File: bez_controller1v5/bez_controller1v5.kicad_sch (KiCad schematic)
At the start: 75 parts, among them J1 Conn_01x03_Male, J10 IMU Conn_01x03_Female, J11 Conn_01x03_Male, J12 Conn_01x03_Male, J13 USB_B_Mini, J2 Conn_01x03_Male, J3 Conn_01x03_Male, J4 Screw_Terminal_01x02, J5 Conn_01x03_Male, J6 Conn_01x03_Male, J7 Conn_01x03_Male, J8 JTAG Conn_01x06_Male, J9 IMU Conn_01x08_Female, U1 PX07806-500-S, U10 USBLC6-4SC6, U11 74LVC2G241, U12 74LVC2G241, U2 74LVC2G241, U3 74LVC2G241, U4 LF50ABV_TO220, U5 LD1117AS33TR_SOT223, U6 INA180A1, U7 STM32F446RETx, U8 74LVC2G241, U9 74LVC2G241, Y1 8MHz

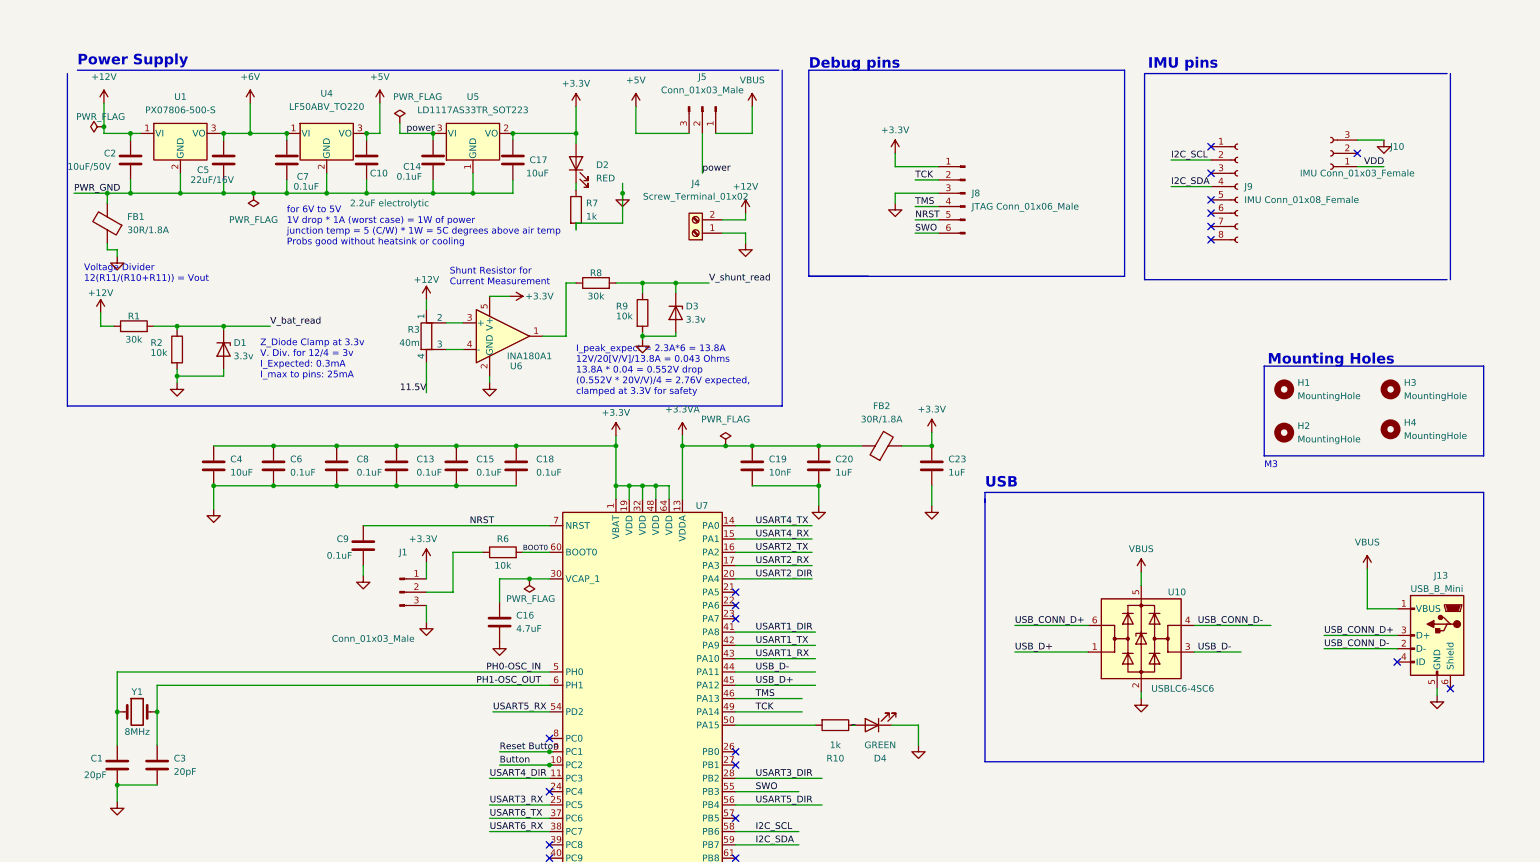
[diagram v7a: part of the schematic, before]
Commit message: Added connection for Voltage Measurement and Current Measurement, also cleaned up PCB a little more
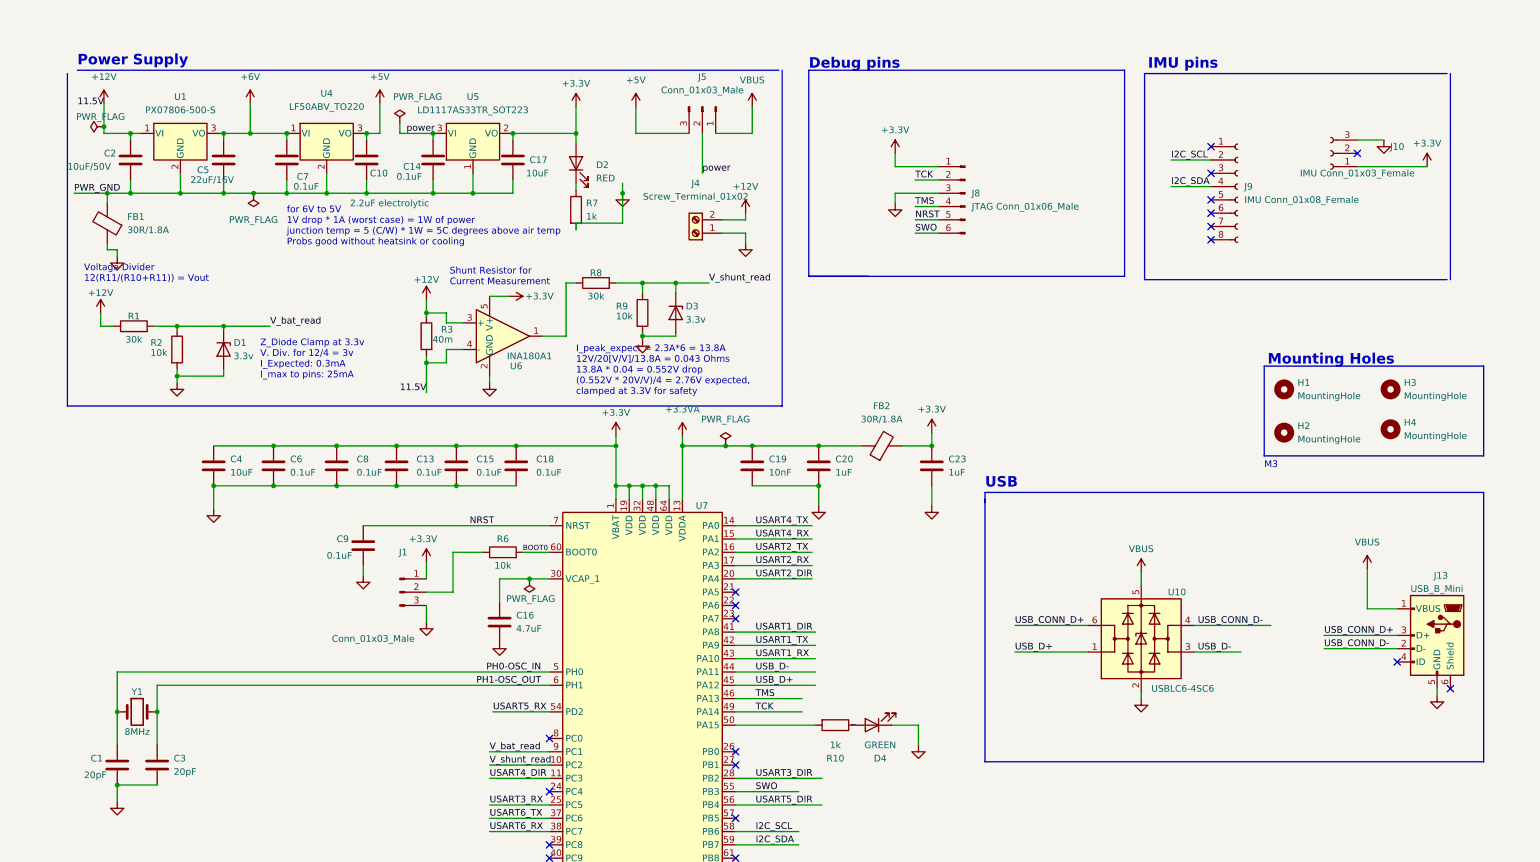
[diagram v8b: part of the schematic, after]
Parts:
- removed R3: 40m, Resistor_SMD:R_0603_1608Metric, symbol Device:R_Shunt
- added R3: 40m, Resistor_SMD:R_0603_1608Metric, symbol Device:R
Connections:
- net Button is gone; now on net V_shunt_read: U7.10 (PC2)
- net Reset Button is gone; now on net V_bat_read: U7.9 (PC1)
- net VDD is gone; now on net +3.3V: J10.1 (Pin_1)
- net +12V: now also U6.3 (+), U6.4 (-), R3.1, R3.2
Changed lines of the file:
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@@
   (junction (at 133.35 -45.085) (diameter 0) (color 0 0 0 0)
   )
+  (junction (at 81.28 73.025) (diameter 0) (color 0 0 0 0)
+  )
   (junction (at 97.79 29.21) (diameter 0) (color 0 0 0 0)
   )
@@
   (junction (at 259.715 -118.11) (diameter 0) (color 0 0 0 0)
   )
-  (junction (at 104.775 147.32) (diameter 0) (color 0 0 0 0)
-  )
   (junction (at 118.745 40.64) (diameter 0) (color 0 0 0 0)
   )
@@
   (junction (at 257.81 -53.34) (diameter 0) (color 0 0 0 0)
   )
+  (junction (at 81.28 63.5) (diameter 0) (color 0 0 0 0)
+  )
   (junction (at 142.875 -102.235) (diameter 0) (color 0 0 0 0)
   )
@@
   (junction (at 135.255 -102.235) (diameter 0) (color 0 0 0 0)
   )
-  (junction (at 104.775 149.86) (diameter 0) (color 0 0 0 0)
-  )
   (junction (at 117.475 88.9) (diameter 0) (color 0 0 0 0)
   )
@@
     (stroke (width 0) (type default))
   )
-  (wire (pts (xy 81.28 60.96) (xy 81.28 62.865))
+  (wire (pts (xy 81.28 60.96) (xy 81.28 63.5))
     (stroke (width 0) (type default))
   )
@@
     (stroke (width 0) (type default))
   )
+  (wire (pts (xy 85.09 70.485) (xy 85.09 73.025))
+    (stroke (width 0) (type default))
+  )
   (wire (pts (xy 41.275 -108.585) (xy 45.72 -108.585))
     (stroke (width 0) (type default))
@@
     (stroke (width 0) (type default))
   )
+  (wire (pts (xy 81.28 71.755) (xy 81.28 73.025))
+    (stroke (width 0) (type default))
+  )
   (wire (pts (xy 81.915 -66.675) (xy 81.915 -45.085))
     (stroke (width 0) (type default))
@@
     (stroke (width 0) (type default))
   )
-  (wire (pts (xy 95.25 149.86) (xy 104.775 149.86))
+  (wire (pts (xy 140.335 182.88) (xy 155.575 182.88))
     (stroke (width 0) (type default))
   )
-  (wire (pts (xy 140.335 182.88) (xy 155.575 182.88))
+  (wire (pts (xy 81.28 63.5) (xy 81.28 64.135))
     (stroke (width 0) (type default))
   )
@@
     (stroke (width 0) (type default))
   )
+  (wire (pts (xy 85.09 73.025) (xy 81.28 73.025))
+    (stroke (width 0) (type default))
+  )
   (wire (pts (xy 174.625 48.26) (xy 179.07 48.26))
     (stroke (width 0) (type default))
@@
     (stroke (width 0) (type default))
   )
-  (wire (pts (xy 19.685 27.94) (xy 19.685 23.495))
+  (wire (pts (xy 19.685 23.495) (xy 19.685 27.94))
     (stroke (width 0) (type default))
   )
@@
     (stroke (width 0) (type default))
   )
-  (wire (pts (xy 95.25 147.32) (xy 104.775 147.32))
-    (stroke (width 0) (type default))
-  )
   (wire (pts (xy 121.285 29.21) (xy 131.445 29.21))
     (stroke (width 0) (type default))
@@
     (stroke (width 0) (type default))
   )
-  (wire (pts (xy 104.775 147.32) (xy 105.41 147.32))
+  (wire (pts (xy 93.345 147.32) (xy 104.775 147.32))
     (stroke (width 0) (type default))
   )
@@
     (stroke (width 0) (type default))
   )
-  (wire (pts (xy 104.775 149.86) (xy 105.41 149.86))
+  (wire (pts (xy 93.345 149.86) (xy 104.775 149.86))
     (stroke (width 0) (type default))
   )
@@
     (stroke (width 0) (type default))
   )
-  (wire (pts (xy 259.08 35.56) (xy 264.16 35.56))
+  (wire (pts (xy 259.08 35.56) (xy 272.415 35.56))
     (stroke (width 0) (type default))
   )
@@
     (stroke (width 0) (type default))
   )
+  (wire (pts (xy 85.09 63.5) (xy 81.28 63.5))
+    (stroke (width 0) (type default))
+  )
   (wire (pts (xy 140.335 127) (xy 155.575 127))
     (stroke (width 0) (type default))
@@
     (stroke (width 0) (type default))
   )
+  (wire (pts (xy 85.09 65.405) (xy 85.09 63.5))
+    (stroke (width 0) (type default))
+  )
   (wire (pts (xy 69.85 38.1) (xy 69.85 40.64))
     (stroke (width 0) (type default))
@@
     (effects (font (size 1.27 1.27)) (justify left bottom))
   )
-  (label "Reset Button" (at 95.25 147.32 0) (fields_autoplaced)
-    (effects (font (size 1.27 1.27)) (justify left bottom))
-  )
   (label "MOTOR_DATA1" (at 57.785 -102.235 0) (fields_autoplaced)
     (effects (font (size 1.27 1.27)) (justify left bottom))
@@
     (effects (font (size 1.27 1.27)) (justify left bottom))
   )
+  (label "11.5V" (at 19.685 24.13 180) (fields_autoplaced)
+    (effects (font (size 1.27 1.27)) (justify right bottom))
+  )
   (label "TCK" (at 174.625 38.1 0) (fields_autoplaced)
     (effects (font (size 1.27 1.27)) (justify left bottom))
@@
     (effects (font (size 1.27 1.27)) (justify left bottom))
   )
+  (label "V_shunt_read" (at 93.345 149.86 0) (fields_autoplaced)
+    (effects (font (size 1.27 1.27)) (justify left bottom))
+  )
   (label "MOTOR_DATA3" (at 245.11 -102.235 0) (fields_autoplaced)
     (effects (font (size 1.27 1.27)) (justify left bottom))
@@
     (effects (font (size 1.27 1.27)) (justify left bottom))
   )
+  (label "V_bat_read" (at 93.345 147.32 0) (fields_autoplaced)
+    (effects (font (size 1.27 1.27)) (justify left bottom))
+  )
   (label "USART6_TX" (at 93.345 160.02 0) (fields_autoplaced)
     (effects (font (size 1.27 1.27)) (justify left bottom))
@@
     (effects (font (size 1.27 1.27)) (justify left bottom))
   )
-  (label "Button" (at 95.25 149.86 0) (fields_autoplaced)
-    (effects (font (size 1.27 1.27)) (justify left bottom))
-  )
   (label "SWO" (at 174.625 48.26 0) (fields_autoplaced)
     (effects (font (size 1.27 1.27)) (justify left bottom))
@@
     (effects (font (size 1.27 1.27)) (justify left bottom))
   )
-  (label "VDD" (at 260.35 35.56 0) (fields_autoplaced)
-    (effects (font (size 1.27 1.27)) (justify left bottom))
-  )
   (symbol (lib_id "power:GND") (at 247.65 -118.11 270) (unit 1)
     (in_bom yes) (on_board yes) (dnp no) (fields_autoplaced)
@@
     )
   )
-  (symbol (lib_id "Device:R_Shunt") (at 81.28 67.945 0) (unit 1)
-    (in_bom yes) (on_board yes) (dnp no)
-    (property "Reference" "R3" (at 80.01 66.675 0)
-      (effects (font (size 1.27 1.27)) (justify right))
-    )
-    (property "Value" "40m" (at 80.01 69.215 0)
-      (effects (font (size 1.27 1.27)) (justify right))
-    )
-    (property "Footprint" "Resistor_SMD:R_0603_1608Metric" (at 79.502 67.945 90)
-      (effects (font (size 1.27 1.27)) hide)
-    )
-    (property "Datasheet" "~" (at 81.28 67.945 0)
-      (effects (font (size 1.27 1.27)) hide)
-    )
-    (pin "1")
-    (pin "2")
-    (pin "3")
-    (pin "4")
-    (instances
-      (project "bez_controller1v5"
-        (path "/f1f9e721-9072-4626-979b-e86715e2d8d4"
-          (reference "R3") (unit 1)
-        )
-      )
-    )
-  )
   (symbol (lib_id "74xGxx:74LVC2G241") (at 133.35 -52.705 0) (mirror x) (unit 2)
     (in_bom yes) (on_board yes) (dnp no) (fields_autoplaced)
@@
     )
   )
+  (symbol (lib_id "power:+3.3V") (at 272.415 35.56 0) (mirror y) (unit 1)
+    (in_bom yes) (on_board yes) (dnp no)
+    (property "Reference" "#PWR061" (at 272.415 39.37 0)
+      (effects (font (size 1.27 1.27)) hide)
+    )
+    (property "Value" "+3.3V" (at 272.415 31.115 0)
+      (effects (font (size 1.27 1.27)))
+    )
+    (property "Footprint" "" (at 272.415 35.56 0)
+      (effects (font (size 1.27 1.27)) hide)
+    )
+    (property "Datasheet" "" (at 272.415 35.56 0)
+      (effects (font (size 1.27 1.27)) hide)
+    )
+    (pin "1")
+    (instances
+      (project "bez_controller1v5"
+        (path "/f1f9e721-9072-4626-979b-e86715e2d8d4"
+          (reference "#PWR061") (unit 1)
+        )
+      )
+    )
+  )
   (symbol (lib_id "Device:C") (at 82.55 34.29 0) (unit 1)
     (in_bom yes) (on_board yes) (dnp no)
@@
         )
       )
+    )
+  )
+  (symbol (lib_id "Device:R") (at 81.28 67.945 0) (mirror y) (unit 1)
+    (in_bom yes) (on_board yes) (dnp no)
+    (property "Reference" "R3" (at 86.36 66.675 0)
+      (effects (font (size 1.27 1.27)) (justify left))
+    )
+    (property "Value" "40m" (at 86.36 68.58 0)
+      (effects (font (size 1.27 1.27)) (justify left))
+    )
+    (property "Footprint" "Resistor_SMD:R_0603_1608Metric" (at 83.058 67.945 90)
+      (effects (font (size 1.27 1.27)) hide)
+    )
+    (property "Datasheet" "~" (at 81.28 67.945 0)
+      (effects (font (size 1.27 1.27)) hide)
+    )
+    (pin "1")
+    (pin "2")
+    (instances
+      (project "bez_controller1v5"
+        (path "/f1f9e721-9072-4626-979b-e86715e2d8d4"
+          (reference "R3") (unit 1)
+        )
+      )
